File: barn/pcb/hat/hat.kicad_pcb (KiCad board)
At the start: 2 copper layers, 61.6 x 84.8 mm, 19 parts, among them J1 Conn_01x02, J2 Conn_01x04, J3 Conn_02x13_Odd_Even, J4 Conn_01x02, J5 Conn_01x02, J6 Conn_01x02, Q1 BC547, Q2 BC547, SW1 SW_Push_DPDT, U1 buck-converter

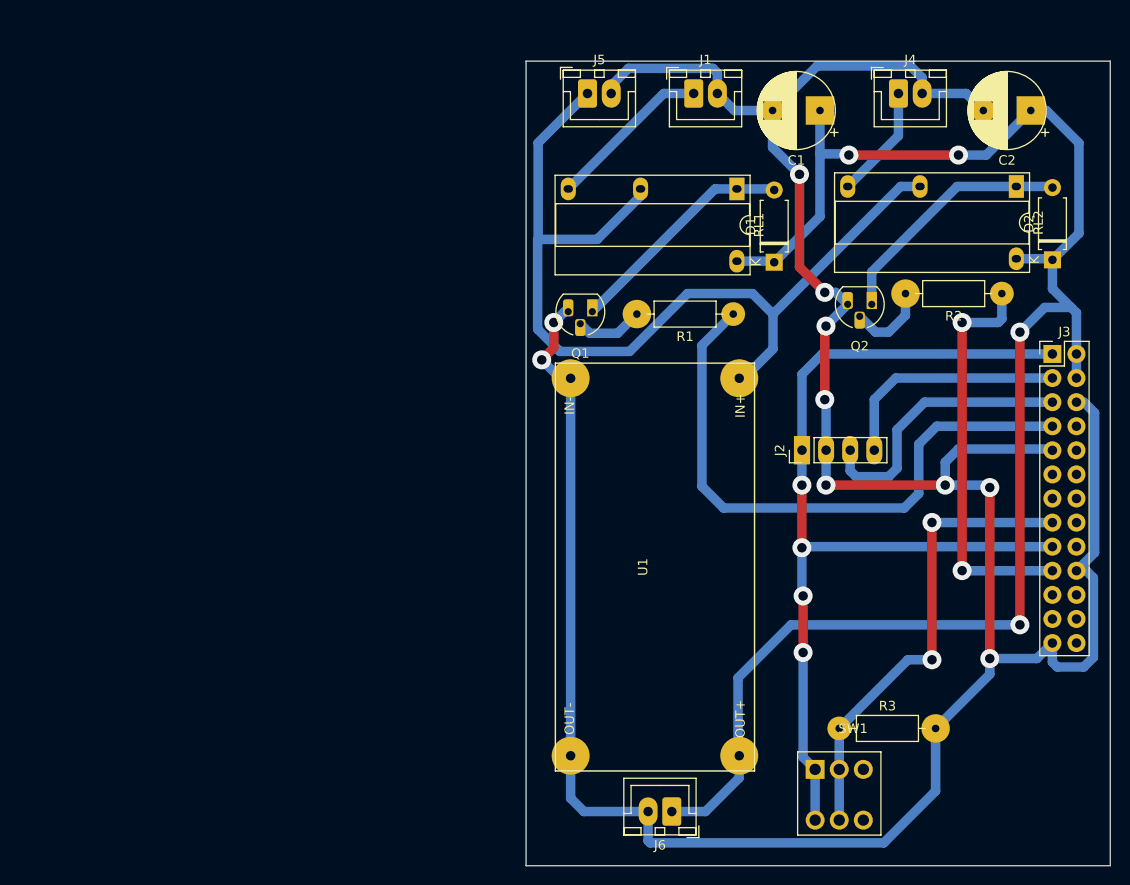
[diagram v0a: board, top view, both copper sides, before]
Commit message: Finish routing.
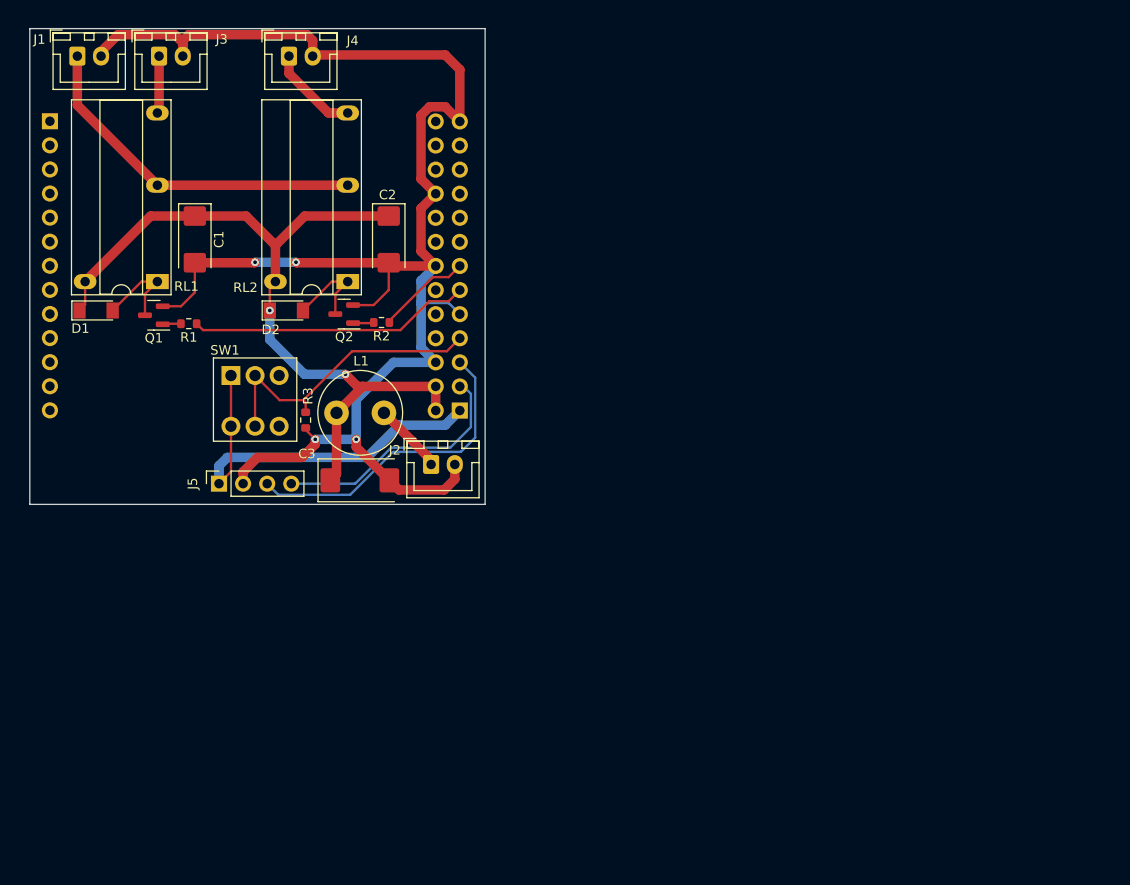
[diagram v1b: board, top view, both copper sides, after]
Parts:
- removed U1: buck-converter, legacy:buck-converter
- added C3: 100u/16V, Capacitor_Tantalum_SMD:CP_EIA-7343-43_Kemet-X, F.Cu at (82.7, 117.9)
- added J7: Conn_01x13, Connector_PinSocket_2.54mm:PinSocket_1x13_P2.54mm_Vertical, B.Cu at (50.0, 80.0)
- added L1: 10m, Inductor_THT:L_Radial_D8.7mm_P5.00mm_Fastron_07HCP, F.Cu at (85.2, 110.7)
- C1, C2: footprint Capacitor_THT:CP_Radial_D8.0mm_P5.00mm -> Capacitor_Tantalum_SMD:CP_EIA-6032-28_Kemet-C
- D1, D2: footprint Diode_THT:D_A-405_P7.62mm_Horizontal -> Diode_SMD:D_MiniMELF
- J2: value Conn_01x04 -> Conn_01x02; footprint Connector_PinHeader_2.54mm:PinHeader_1x04_P2.54mm_Vertical -> Connector_JST:JST_XH_B2B-XH-A_1x02_P2.50mm_Vertical
- J3: value Conn_02x13_Odd_Even -> Conn_01x02; footprint Connector_PinHeader_2.54mm:PinHeader_2x13_P2.54mm_Vertical -> Connector_JST:JST_XH_B2B-XH-A_1x02_P2.50mm_Vertical
- J5: value Conn_01x02 -> Conn_01x04; footprint Connector_JST:JST_XH_B2B-XH-A_1x02_P2.50mm_Vertical -> Connector_PinSocket_2.54mm:PinSocket_1x04_P2.54mm_Vertical
- J6: value Conn_01x02 -> Conn_02x13_Odd_Even; footprint Connector_JST:JST_XH_B2B-XH-A_1x02_P2.50mm_Vertical -> Connector_PinSocket_2.54mm:PinSocket_2x13_P2.54mm_Vertical; moved to B.Cu
- Q1, Q2: value BC547 -> MMBT3904; footprint Package_TO_SOT_THT:TO-92_HandSolder -> Package_TO_SOT_SMD:SOT-23
- R1, R2, R3: footprint Resistor_THT:R_Axial_DIN0207_L6.3mm_D2.5mm_P10.16mm_Horizontal -> Resistor_SMD:R_0603_1608Metric
- moved J3 99.3 mm to (61.5, 73.1)
- moved D2 80.9 mm to (74.9, 99.9), turned to 0 degrees
- moved SW1 74.3 mm to (69.1, 106.8)
- moved D1 71.7 mm to (54.9, 99.9), turned to 0 degrees
- moved RL2 71.2 mm to (81.4, 96.9), turned to 180 degrees
- moved C2 69.0 mm to (85.7, 92.5), turned to -90 degrees
- moved C1 67.3 mm to (65.3, 92.5), turned to -90 degrees
- moved R2 65.5 mm to (85.0, 101.2)
- moved J1 65.1 mm to (52.9, 73.1)
- moved R3 65.0 mm to (77.0, 111.5), turned to -90 degrees
- moved J4 64.4 mm to (75.2, 73.1)
- moved RL1 61.9 mm to (61.3, 96.9), turned to 180 degrees
- moved R1 57.4 mm to (64.6, 101.3)
- moved J5 56.6 mm to (67.8, 118.2), turned to 90 degrees
- moved Q2 55.6 mm to (81.0, 100.3)
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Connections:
- J1 pad 1: Net-(J1-Pad1) -> +12V
- J2 pad 1: +3V3 -> Net-(J2-Pad1)
- J3 pad 1: +3V3 -> Net-(J3-Pad1)
- J3 pad 2: +5V -> GND
- J5 pad 1: +12V -> +3V3
- J6 pad 1: +5V -> +3V3
- J6 pad 2: GND -> +5V
- Q1 pad 1: Net-(D1-Pad2) -> Net-(Q1-Pad1)
- Q1 pad 2: Net-(R1-Pad2) -> GND
- Q1 pad 3: GND -> Net-(D1-Pad2)
- Q2 pad 1: Net-(D2-Pad2) -> Net-(Q2-Pad1)
- Q2 pad 2: Net-(R2-Pad2) -> GND
- Q2 pad 3: GND -> Net-(D2-Pad2)
- R1 pad 1: GPIO4 -> GPIO1
- R1 pad 2: Net-(R1-Pad2) -> Net-(Q1-Pad1)
- R2 pad 1: GPIO10 -> GPIO0
- R2 pad 2: Net-(R2-Pad2) -> Net-(Q2-Pad1)
- R3 pad 1: GPIO22 -> GPIO6
- RL1 pad 4: Net-(J1-Pad1) -> Net-(J3-Pad1)
- SW1 pad 2: GPIO22 -> GPIO6
- SW1 pad 5: GPIO22 -> GPIO6
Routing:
- net GND: track 303.0 -> 175.4 mm, vias 10 -> 4
- net +5V: track 172.1 -> 84.3 mm, vias 4 -> 2
- net GPIO4: track 64.0 -> 0.00 mm
- net +12V: track 99.3 -> 37.2 mm
- net +3V3: track 101.3 -> 41.6 mm, vias 4 -> 0
- net GPIO22: track 49.6 -> 0.00 mm, vias 2 -> 0
- net GPIO10: track 42.7 -> 0.00 mm, vias 2 -> 0
- net GPIO6: track 0.00 -> 32.1 mm
- net GPIO1: track 0.00 -> 29.8 mm
- net Net-(J1-Pad1): track 17.4 -> 0.00 mm
- net Net-(D2-Pad2): track 26.2 -> 9.94 mm
- net Net-(D1-Pad2): track 24.6 -> 10.1 mm
- net GPIO0: track 0.00 -> 10.0 mm
- net Net-(R2-Pad2): track 8.54 -> 0.00 mm
- net Net-(J2-Pad1): track 0.00 -> 7.50 mm
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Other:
- board size 61.6 x 84.8 mm -> 48 x 50.2 mm

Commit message: Fill zones.
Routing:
- added copper zone on B.Cu, net +5V
- added copper zone on F.Cu, net GND
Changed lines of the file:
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@@
     (fp_line (start 0 -1.35) (end 0.625 -2.35) (layer "F.Fab") (width 0.1))
     (fp_line (start 4.95 -2.35) (end -2.45 -2.35) (layer "F.Fab") (width 0.1))
-    (pad "1" thru_hole roundrect (at 0 0) (size 1.7 2) (drill 1) (layers *.Cu *.Mask) (roundrect_rratio 0.147059)
+    (pad "1" thru_hole roundrect (at 0 0) (size 1.7 2) (drill 1) (layers *.Cu *.Mask) (roundrect_rratio 0.1470588235)
       (net 5 "Net-(J2-Pad1)") (pinfunction "Pin_1") (pintype "passive"))
     (pad "2" thru_hole oval (at 2.5 0) (size 1.7 2) (drill 1) (layers *.Cu *.Mask)
@@
     (fp_line (start -2.45 -2.35) (end -2.45 3.4) (layer "F.Fab") (width 0.1))
     (fp_line (start -2.45 3.4) (end 4.95 3.4) (layer "F.Fab") (width 0.1))
-    (pad "1" thru_hole roundrect (at 0 0) (size 1.7 2) (drill 1) (layers *.Cu *.Mask) (roundrect_rratio 0.147059)
+    (pad "1" thru_hole roundrect (at 0 0) (size 1.7 2) (drill 1) (layers *.Cu *.Mask) (roundrect_rratio 0.1470588235)
       (net 17 "Net-(J3-Pad1)") (pinfunction "Pin_1") (pintype "passive"))
     (pad "2" thru_hole oval (at 2.5 0) (size 1.7 2) (drill 1) (layers *.Cu *.Mask)
@@
   (segment (start 93.218 95.26) (end 92.043489 96.434511) (width 0.25) (layer "F.Cu") (net 18))
   (segment (start 85.788 101.029) (end 85.788 101.219) (width 0.25) (layer "F.Cu") (net 18))
+  (zone (net 2) (net_name "GND") (layer "F.Cu") (hatch edge 0.508)
+    (connect_pads (clearance 0.508))
+    (min_thickness 0.254) (filled_areas_thickness no)
+    (fill yes (thermal_gap 0.508) (thermal_bridge_width 0.508))
+    (polygon
+      (pts
+        (xy 96.266 120.904)
+        (xy 46.99 120.904)
+        (xy 46.99 69.215)
+        (xy 96.266 69.215)
+      )
+    )
+  )
+  (zone (net 1) (net_name "+5V") (layer "B.Cu") (hatch edge 0.508)
+    (connect_pads (clearance 0.508))
+    (min_thickness 0.254) (filled_areas_thickness no)
+    (fill yes (thermal_gap 0.508) (thermal_bridge_width 0.508))
+    (polygon
+      (pts
+        (xy 97.409 121.666)
+        (xy 46.863 121.666)
+        (xy 46.736 69.215)
+        (xy 46.863 69.342)
+        (xy 97.409 69.215)
+      )
+    )
+  )
 )

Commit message: Add input for door switch.
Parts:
- removed L1: 10m, Inductor_THT:L_Radial_D8.7mm_P5.00mm_Fastron_07HCP
- added C4: 100n, Capacitor_SMD:C_0603_1608Metric, F.Cu at (84.6, 76.7)
- added J8: Conn_01x02, Connector_JST:JST_XH_B2B-XH-A_1x02_P2.50mm_Vertical, F.Cu at (89.4, 73.1)
- added R4: 1K, Resistor_SMD:R_0603_1608Metric, F.Cu at (84.6, 72.6)
- added R5: 1K, Resistor_SMD:R_0603_1608Metric, F.Cu at (84.6, 74.7)
- R3: value 10K -> 1K
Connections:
- J2 pad 1: Net-(J2-Pad1) -> +5V
- J6 pad 15: unconnected-(J6-Pad15) -> GPIO3
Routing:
- net +3V3: track 41.6 -> 88.1 mm, vias 0 -> 1
- net GPIO3: track 0.00 -> 22.9 mm, vias 0 -> 1
- net GND: track 175.4 -> 186.0 mm
- net Net-(J2-Pad1): track 7.50 -> 0.00 mm
- net +5V: track 84.3 -> 90.7 mm
- net Net-(J8-Pad1): track 0.00 -> 6.26 mm

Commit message: Adjust edge cuts.
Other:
- board size 48 x 50.2 mm -> 48 x 49.9 mm
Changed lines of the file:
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@@
     )
   )
-  (gr_rect (start 47.879 70.231) (end 95.885 120.396) (layer "Edge.Cuts") (width 0.1) (fill none))
+  (gr_rect (start 47.879 70.485) (end 95.885 120.396) (layer "Edge.Cuts") (width 0.1) (fill none))
   (segment (start 90.678 107.96) (end 90.678 110.5) (width 1) (layer "F.Cu") (net 1))
   (segment (start 73.18 99.949) (end 73.18 97.503) (width 0.25) (layer "F.Cu") (net 1))
